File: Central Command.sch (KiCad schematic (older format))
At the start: 12 parts, among them P101 CONN_01X10, P102 CONN_01X10, P103 CONN_01X04, P104 CONN_01X02, P105 CONN_01X04, P106 CONN_01X02, U101 STM32F030C8, Y101 Crystal

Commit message: Changed board outline (now 2x2) and placed headers around the outside based on pin connections.
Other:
- note added: "TODO: Add indicator LEDs"
- note removed: "TODO: Figure out comm/power header"
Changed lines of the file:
@@
 	1    0    0    -1
 $EndComp
-Text Notes 5100 2850 0    60   ~ 0
-TODO: Figure out comm/power header
 $Comp
 L Crystal Y101
@@
 Text Notes 800  4300 0    60   ~ 0
 GPIO HEADER 2
+Text Notes 5100 3050 0    60   ~ 0
+TODO: Add indicator LEDs
 $EndSCHEMATC

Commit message: Added ground and power layers.
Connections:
- net GND: now also C101.2
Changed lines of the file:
@@
 Text Notes 5100 3050 0    60   ~ 0
 TODO: Add indicator LEDs
+$Comp
+L GND #PWR?
+U 1 1 56774FCA
+P 5150 1100
+F 0 "#PWR?" H 5150 850 50  0001 C CNN
+F 1 "GND" H 5150 950 50  0000 C CNN
+F 2 "" H 5150 1100 60  0000 C CNN
+F 3 "" H 5150 1100 60  0000 C CNN
+	1    5150 1100
+	1    0    0    -1
+$EndComp
 $EndSCHEMATC

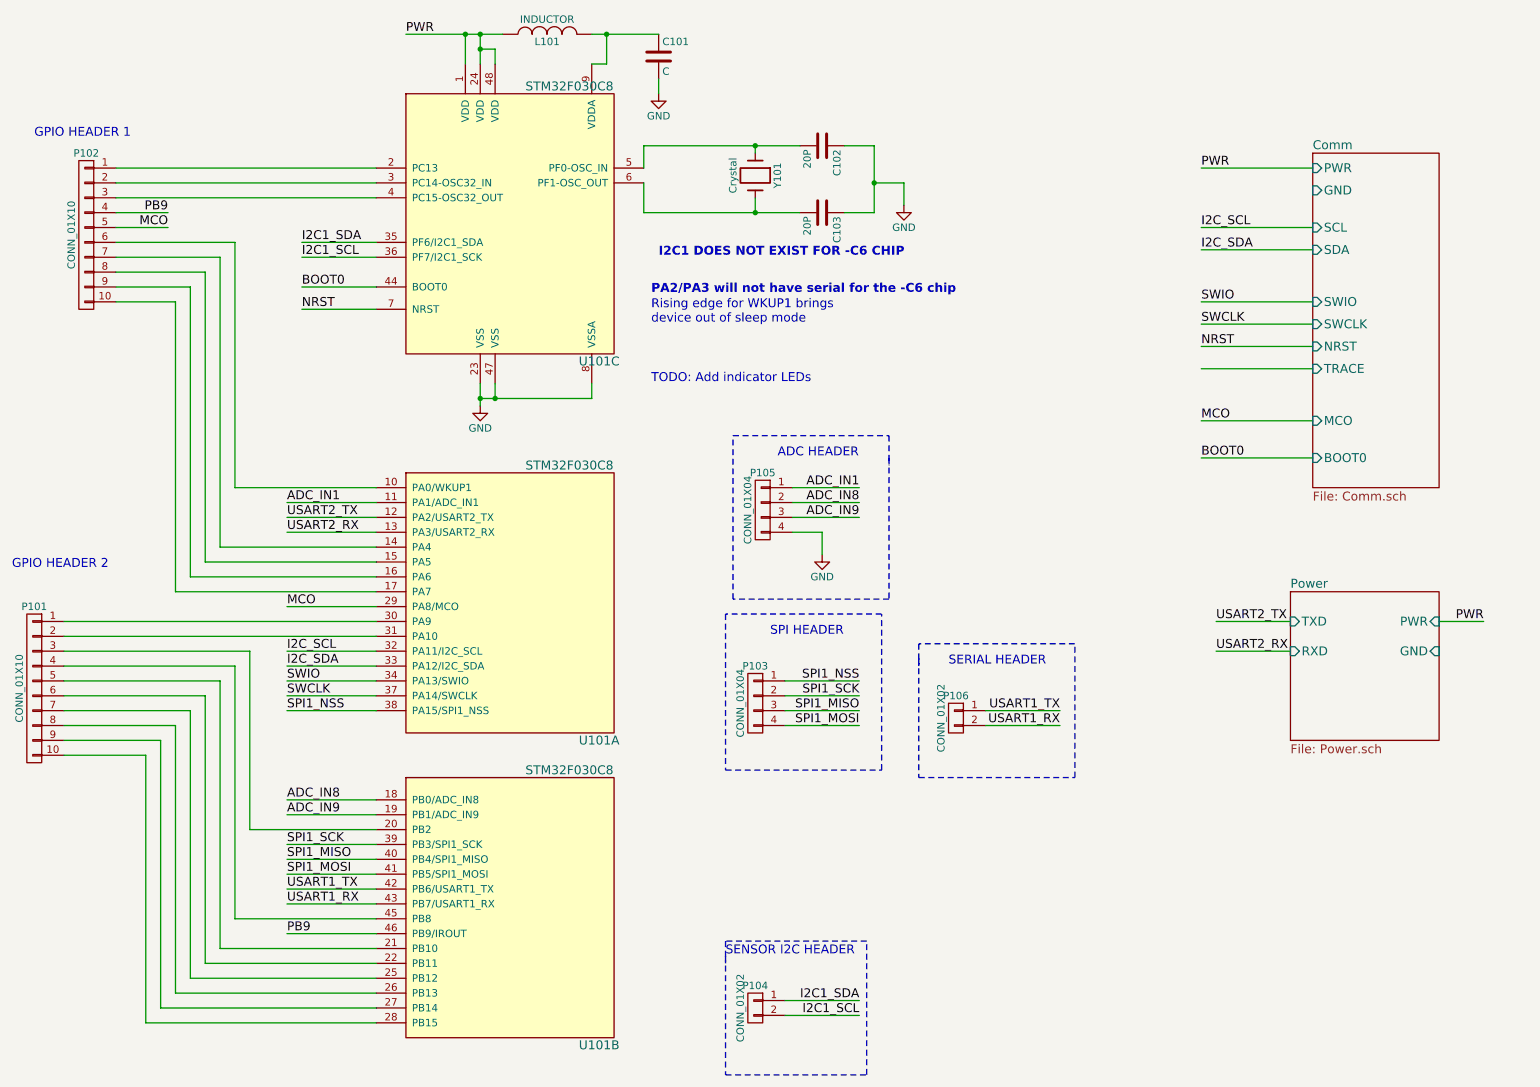
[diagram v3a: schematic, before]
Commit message: Swapped two connectors and routed the bottom connector
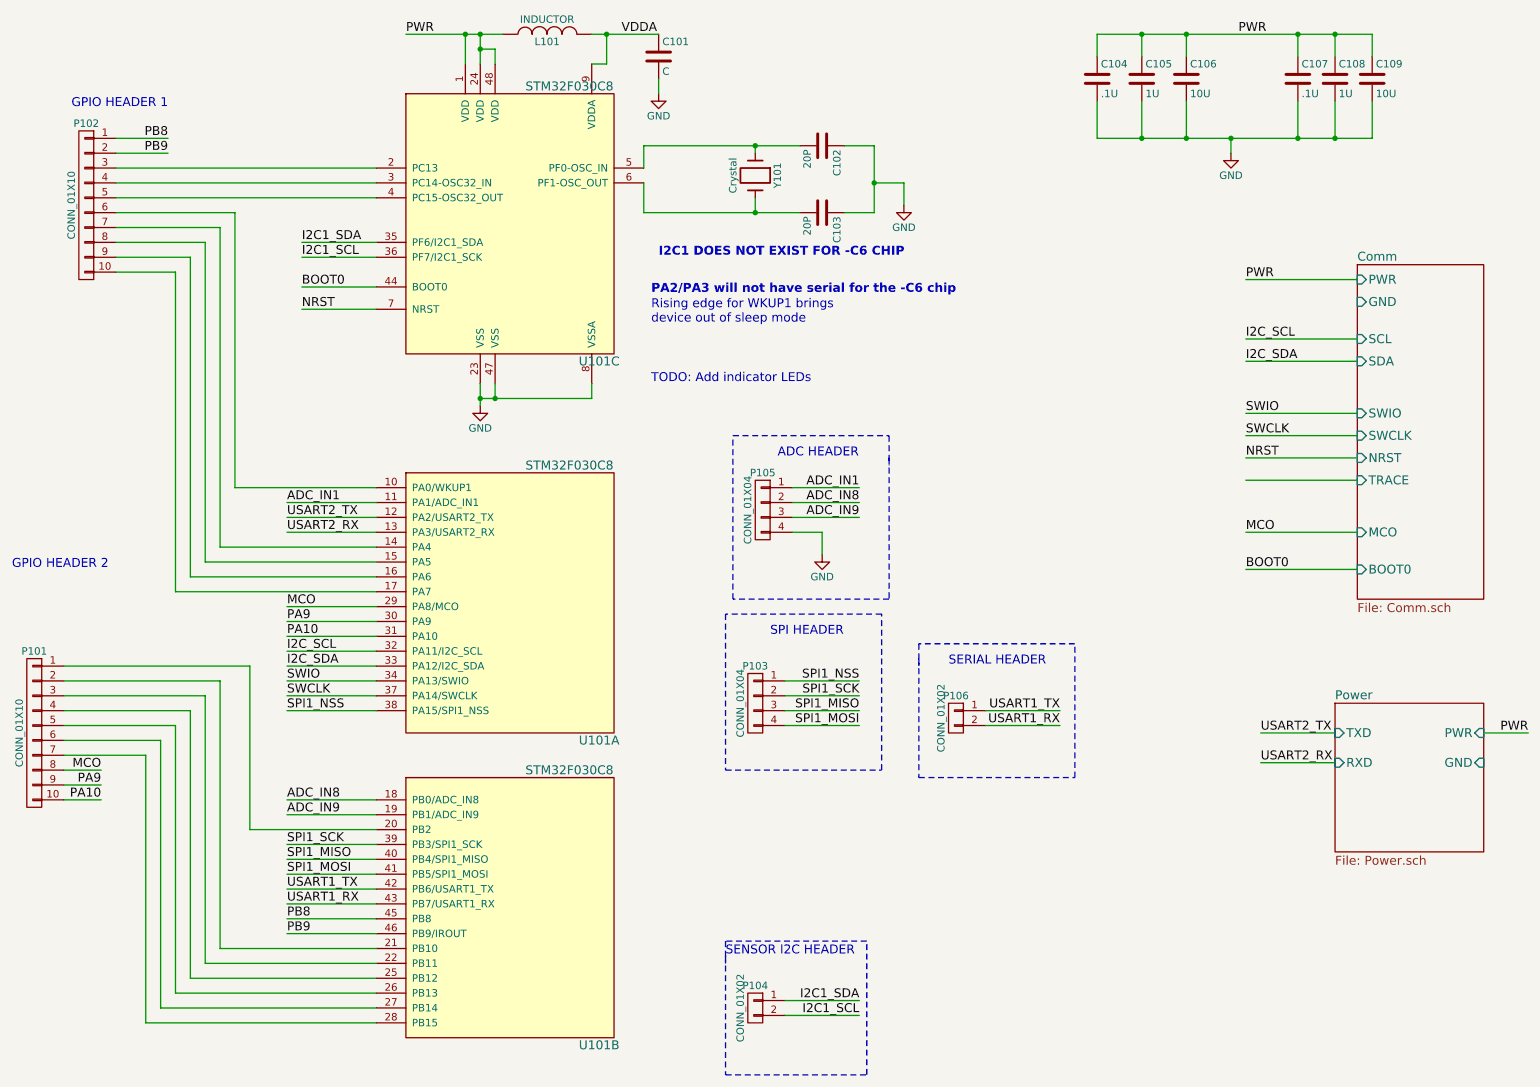
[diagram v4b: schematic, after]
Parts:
- added C104, C107: .1U, Capacitors_SMD:C_0805, symbol C
- added C105, C108: 1U, Capacitors_SMD:C_1206, symbol C
- added C106, C109: 10U, Capacitors_SMD:C_1206, symbol C
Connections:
- net GND: now also C104.2, C105.2, C106.2, C107.2, C108.2, C109.2
- net MCO: now also P101.8 (P8); no longer P102.5 (P5)
- net PB9: now also P102.2 (P2); no longer P102.4 (P4)
- net PWR: now also C104.1, C105.1, C106.1, C107.1, C108.1, C109.1
- net VDDA: now reaches C101.1, L101.2, U101.9 (VDDA)
- net at P101.1 (P1): now also U101.20 (PB2); no longer U101.30 (PA9)
- net at P101.2 (P2): now also U101.21 (PB10); no longer U101.31 (PA10)
- net at P101.3 (P3): now also U101.22 (PB11); no longer U101.20 (PB2)
- net at P101.5 (P5): now also U101.26 (PB13); no longer U101.21 (PB10)
- net at P101.6 (P6): now also U101.27 (PB14); no longer U101.22 (PB11)
- net at U101.25 (PB12): now also P101.4 (P4); no longer P101.7 (P7)
- net PA9: now reaches P101.9 (P9)
- net PA9: now also U101.30 (PA9); no longer U101.27 (PB14)
- net at U101.28 (PB15): now also P101.7 (P7); no longer P101.10 (P10)
- net PB8: now reaches U101.45 (PB8)
- net PB8: now also P102.1 (P1); no longer P101.4 (P4)
- net at U101.2 (PC13): now also P102.3 (P3); no longer P102.1 (P1)
- net at U101.3 (PC14-OSC32_IN): now also P102.4 (P4); no longer P102.2 (P2)
- net at U101.4 (PC15-OSC32_OUT): now also P102.5 (P5); no longer P102.3 (P3)
- new net PA10: P101.10 (P10), U101.31 (PA10)
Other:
- moved on the sheet: P101, P102

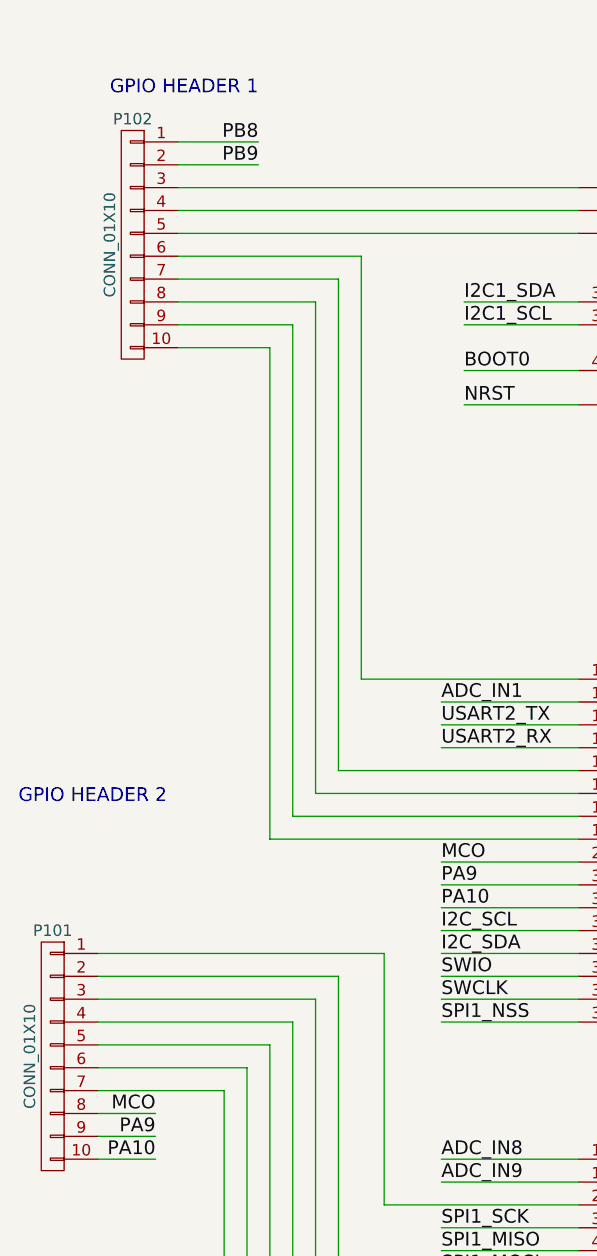
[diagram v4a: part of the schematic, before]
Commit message: Finished layout including labels and DRC
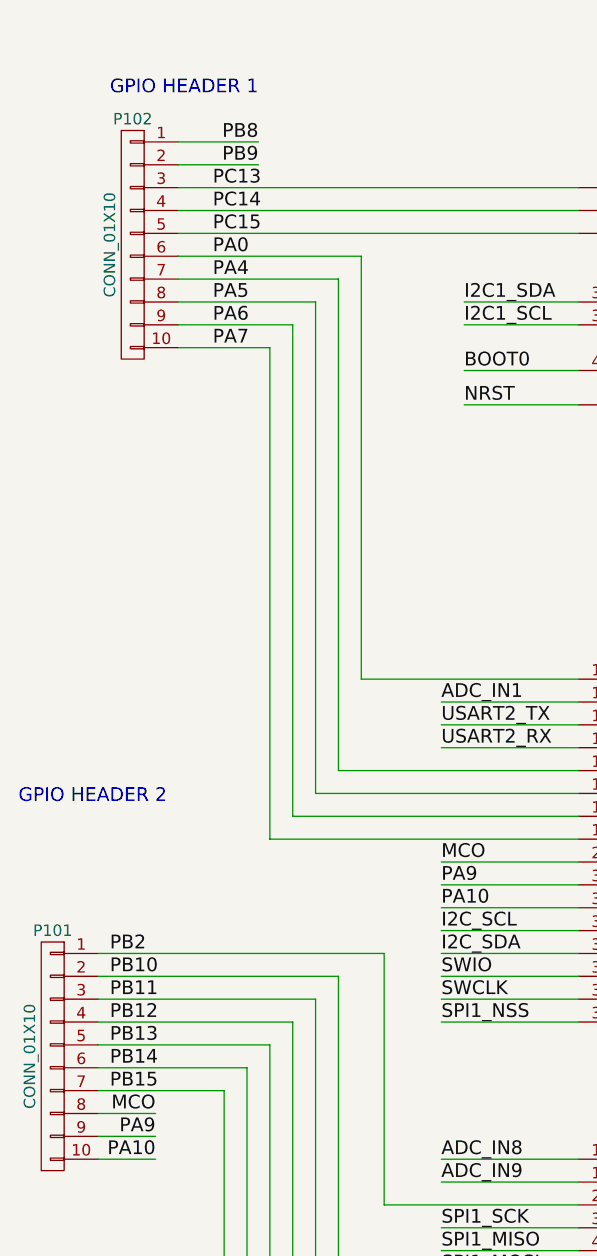
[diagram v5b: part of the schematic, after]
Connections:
- net PA0: now reaches P102.6 (P6), U101.10 (PA0/WKUP1)
- net PA4: now reaches P102.7 (P7), U101.14 (PA4)
- net PA5: now reaches P102.8 (P8), U101.15 (PA5)
- net PA6: now reaches P102.9 (P9), U101.16 (PA6)
- net PA7: now reaches P102.10 (P10), U101.17 (PA7)
- net PB2: now reaches P101.1 (P1), U101.20 (PB2)
- net PB10: now reaches P101.2 (P2), U101.21 (PB10)
- net PB11: now reaches P101.3 (P3), U101.22 (PB11)
- net PB12: now reaches P101.4 (P4), U101.25 (PB12)
- net PB13: now reaches P101.5 (P5), U101.26 (PB13)
- net PB14: now reaches P101.6 (P6), U101.27 (PB14)
- net PB15: now reaches P101.7 (P7), U101.28 (PB15)
- net PC13: now reaches P102.3 (P3), U101.2 (PC13)
- net PC14: now reaches P102.4 (P4), U101.3 (PC14-OSC32_IN)
- net PC15: now reaches P102.5 (P5), U101.4 (PC15-OSC32_OUT)
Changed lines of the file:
@@
 	9950 700  9950 850
 Connection ~ 9700 700
+Text Label 1650 1600 0    60   ~ 0
+PC13
+Text Label 1650 1700 0    60   ~ 0
+PC14
+Text Label 1650 1800 0    60   ~ 0
+PC15
+Text Label 1650 1900 0    60   ~ 0
+PA0
+Text Label 1650 2000 0    60   ~ 0
+PA4
+Text Label 1650 2100 0    60   ~ 0
+PA5
+Text Label 1650 2200 0    60   ~ 0
+PA6
+Text Label 1650 2300 0    60   ~ 0
+PA7
+Text Label 1200 4950 0    60   ~ 0
+PB2
+Text Label 1200 5050 0    60   ~ 0
+PB10
+Text Label 1200 5150 0    60   ~ 0
+PB11
+Text Label 1200 5250 0    60   ~ 0
+PB12
+Text Label 1200 5350 0    60   ~ 0
+PB13
+Text Label 1200 5450 0    60   ~ 0
+PB14
+Text Label 1200 5550 0    60   ~ 0
+PB15
 $EndSCHEMATC
